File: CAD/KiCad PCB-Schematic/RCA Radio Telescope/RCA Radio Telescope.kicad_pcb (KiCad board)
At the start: 2 copper layers, 60 x 40 mm, 23 parts, among them J2 5V From PoE Splitter, J3 3V Out For LNA, J4 5V Out For Filter Board, J7 USB_A, J8 USB_A, Q1 DMP2008UFG-7, U13 MIC23050-SYML-TR, U14 TPS62133RGTR

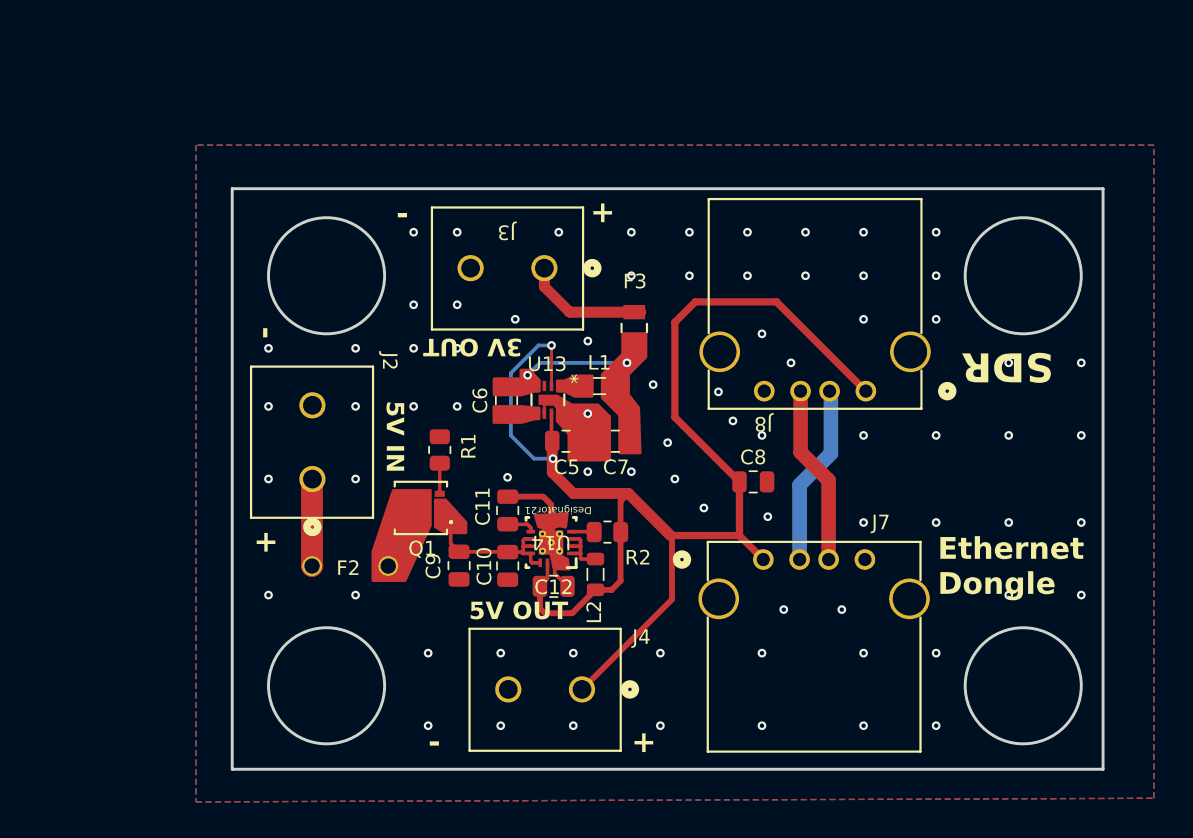
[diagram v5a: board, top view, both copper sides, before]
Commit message: Updated Power/Data Schematic to v1.6 and Power/Data PCB to v1.5
- Added Testpoints to both Schematic and PCB
- Rearranged components on PCB to fit missing diode
- Changed Zener diode and PMOS on Protection Circuit to work with 12V max
- Fixed warnings and errors from DRC
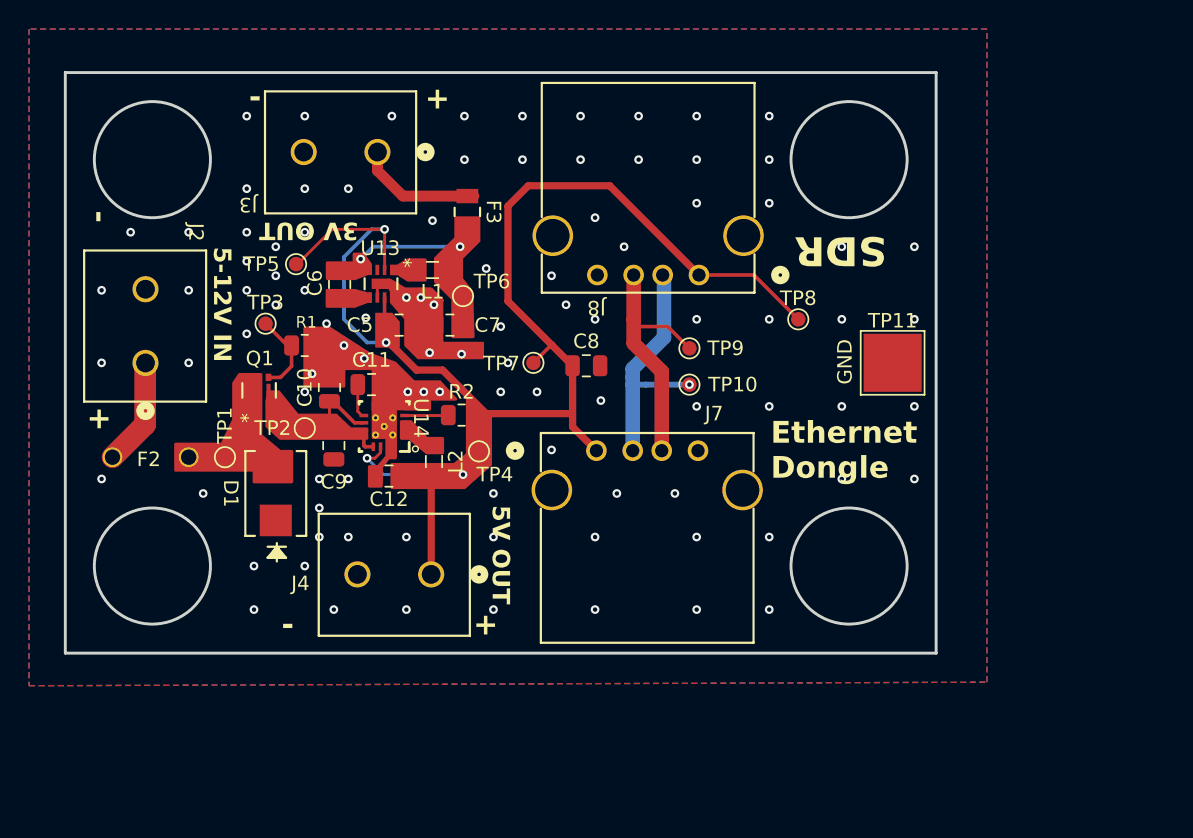
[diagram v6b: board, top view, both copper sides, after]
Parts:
- added D1: SMBJ12A-13-F, Library:SMB_DIO, F.Cu at (28.5, 43.0)
- added TP1: PROCTVIN, TestPoint:TestPoint_Pad_D1.0mm, F.Cu at (25.0, 40.5)
- added TP10: D-USB, TestPoint:TestPoint_Pad_D1.0mm, F.Cu at (57.0, 35.5)
- added TP11: GNDCLIP, TestPoint:TestPoint_Pad_4.0x4.0mm, F.Cu at (71.0, 34.0)
- added TP2: 5VBUCKVIN, TestPoint:TestPoint_Pad_D1.0mm, F.Cu at (30.5, 38.5)
- added TP3: G_PMOS, TestPoint:TestPoint_Pad_D1.0mm, F.Cu at (27.8, 31.3)
- added TP4: 5VBUCKVOUT, TestPoint:TestPoint_Pad_D1.0mm, F.Cu at (42.5, 40.1)
- added TP5: 3VBUCKIN, TestPoint:TestPoint_Pad_D1.0mm, F.Cu at (29.9, 27.2)
- added TP6: 3VBUCKOUT, TestPoint:TestPoint_Pad_D1.0mm, F.Cu at (41.4, 29.4)
- added TP7: 5VOUT, TestPoint:TestPoint_Pad_D1.0mm, F.Cu at (46.2, 34.0)
- added TP8: 5VUSB, TestPoint:TestPoint_Pad_D1.0mm, F.Cu at (64.5, 31.0)
- added TP9: D+USB, TestPoint:TestPoint_Pad_D1.0mm, F.Cu at (57.0, 33.0)
- Q1: value DMP2008UFG-7 -> DMP4047LFDE-7; footprint Library:DMP2008UFG-7_DIO -> Library:U-DFN2020-6_DIO
- U14: footprint TPS62133RGTR:RGT0016C -> Library:RGT0016C
- moved C10 17.4 mm to (32.2, 35.7), turned to 90 degrees
- moved F2 15.7 mm to (20.2, 44.5)
- moved C5 14.0 mm to (37.0, 31.4)
- moved C8 14.0 mm to (49.9, 34.2)
- moved F3 14.0 mm to (41.7, 23.6)
- moved J2 14.0 mm to (19.5, 34.0)
- moved J3 14.0 mm to (35.5, 19.5)
- moved L1 14.0 mm to (39.3, 27.6)
- moved U14 14.0 mm to (36.0, 38.4)
- moved C6 14.0 mm to (32.9, 28.6)
- moved U13 14.0 mm to (35.8, 28.6)
- moved J8 14.0 mm to (57.7, 27.9)
- moved C7 13.9 mm to (40.5, 31.4)
- moved Q1 13.8 mm to (27.3, 35.9), turned to 90 degrees
- moved J7 13.7 mm to (50.6, 40.1)
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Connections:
- U14 pad 18: (no net) -> GND
- U14 pad 19: (no net) -> GND
- U14 pad 20: (no net) -> GND
- U14 pad 21: (no net) -> GND
- U14 pad 22: (no net) -> GND
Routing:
- net GND: track 7.89 -> 1.44 mm, vias 75 -> 98
- net Net-(Q1-S): track 10.9 -> 5.58 mm
- net /PowerDataDistribute/USB_D+_IN: track 12.4 -> 16.9 mm
- net /PowerDataDistribute/USB_D-_IN: track 12.5 -> 16.9 mm, vias 0 -> 1
- net Net-(L2-Pad1): track 4.23 -> 0.00 mm
- net Net-(Q1-G): track 2.11 -> 5.75 mm
- net Net-(U14-PG): track 1.58 -> 3.03 mm
- net /PowerDataDistribute/VDD: track 6.07 -> 7.44 mm
- net +5V: track 97.5 -> 98.1 mm, vias 2 -> 4
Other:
- outline, holes or cut-outs redrawn
- board text added: "5-12V IN"
- board text added: "GND"
- board text added: "PSU ECE Capstone Team 11 - RCA Telescope v1.5"
- board text removed: "5V IN"
- board text removed: "PSU ECE Capstone Team 11 - RCA Telescope v1.1"

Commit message: Updated PowerData PCB to v1.6 and PowerData Schematic to v1.7
- Design Review with Andrew
- Fixed up various parts of PCB parameters
- May consider LDO or filtering for Power IC
- May want to consider a circuit breaker IC for LNA supply
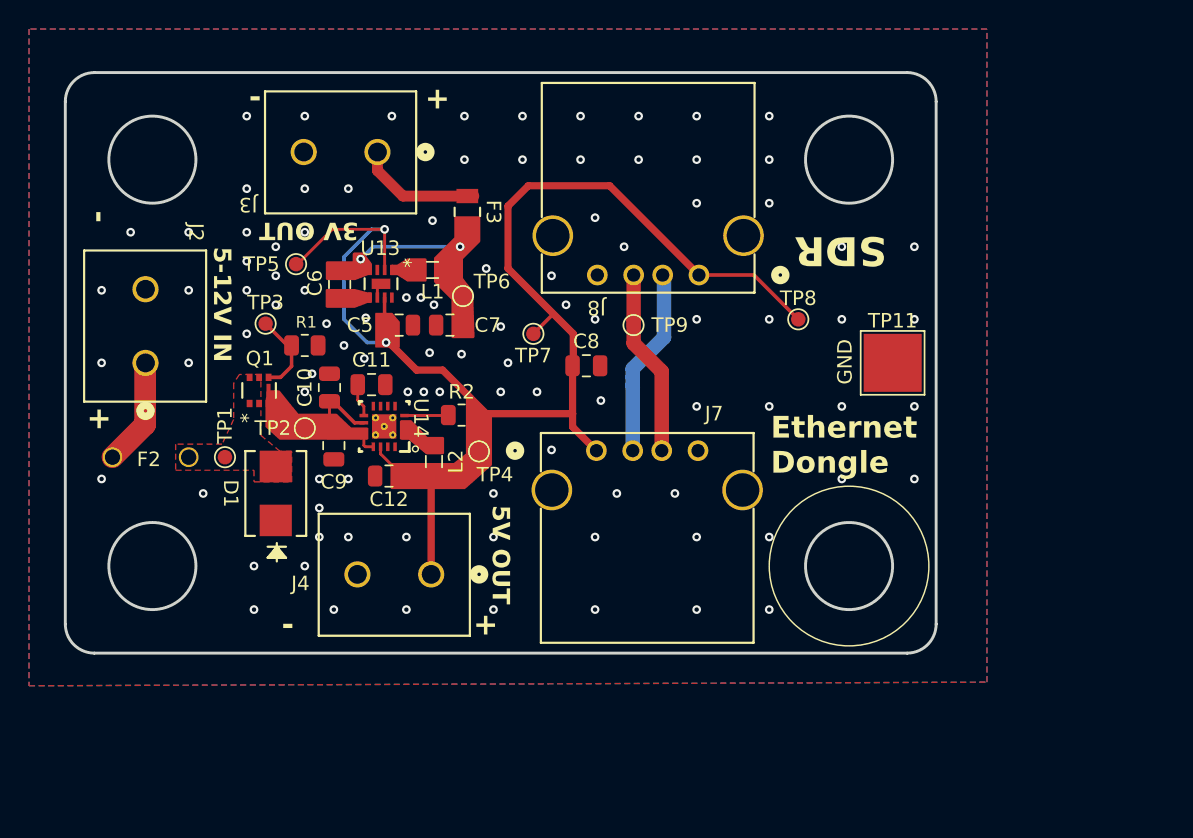
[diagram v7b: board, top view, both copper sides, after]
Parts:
- TP10: moved to B.Cu
- moved TP9 4.17 mm to (53.1, 31.4)
- moved TP10 3.91 mm to (53.1, 35.7), turned to 180 degrees
- moved TP7 2.00 mm to (46.2, 32.0)
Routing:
- net /PowerDataDistribute/USB_D+_IN: track 16.9 -> 12.9 mm
- net /PowerDataDistribute/USB_D-_IN: track 16.9 -> 13.0 mm, vias 1 -> 0
- net +5V: track 98.1 -> 94.3 mm, vias 4 -> 2
- added copper zone on F.Cu, net Net-(Q1-D)
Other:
- outline, holes or cut-outs redrawn
- board text added: "PSU ECE Capstone Team 11 - RCA Telescope v1.6 (3/26/2025)"
- board text removed: "PSU ECE Capstone Team 11 - RCA Telescope v1.5"

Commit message: Updated PowerData Schematic to v1.8 and PCB to v1.7
- Swapped MIC Buck to LDO
- Changed footprint for Buck Inductor to appropriate component
- Rearranged PCB layout to accommodate new inductor
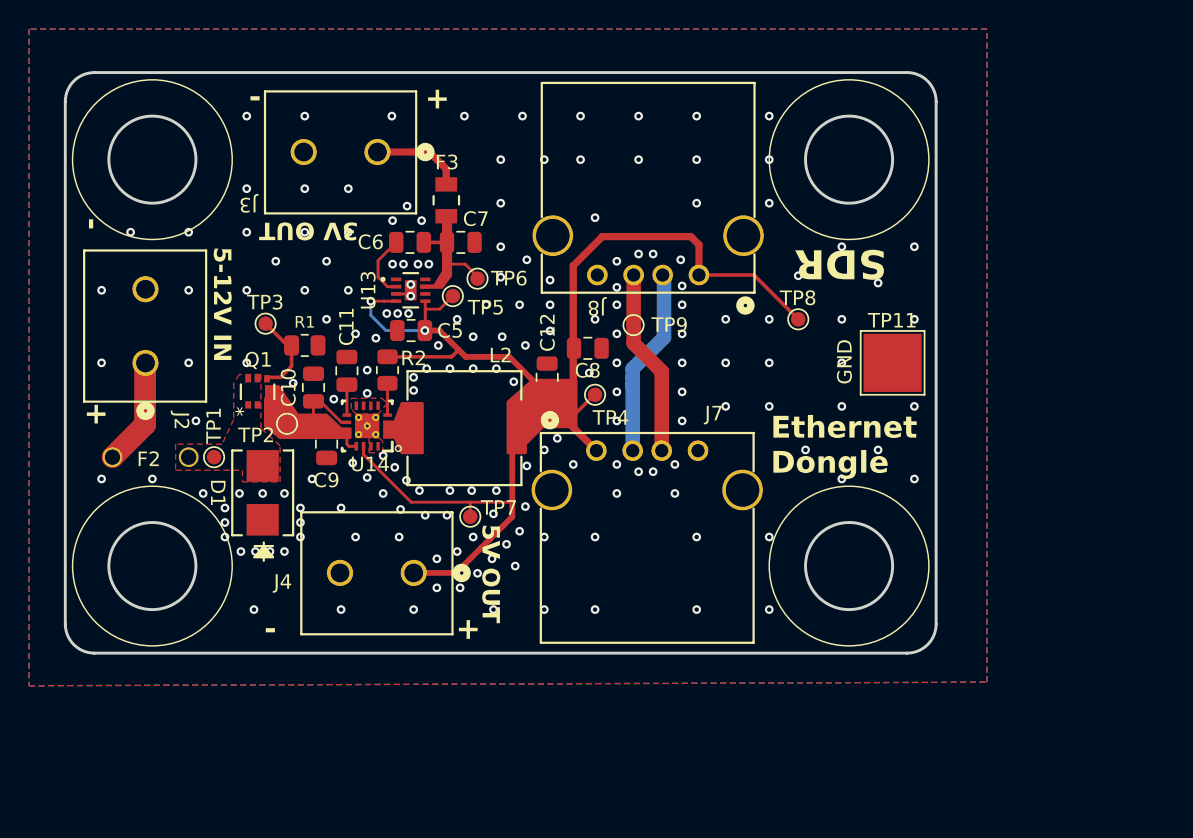
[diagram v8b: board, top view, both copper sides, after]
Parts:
- removed L1: 1 uH, Inductor_SMD:L_0805_2012Metric
- C5, C7: value 4.7 uF -> 1 uF
- C6: value 560 pF -> 10 nf
- L2: footprint Inductor_SMD:L_0805_2012Metric -> Library:IND_CB_DRA73
- TP5: value 3VBUCKIN -> 3VLDOIN
- TP6: value 3VBUCKOUT -> 3VLDOOUT
- U13: value MIC23050-SYML-TR -> MAX8510ETA30+T; footprint Library:MLF-8_ML_MCH -> Library:21-0168E_T822-1_MXM
- moved TP7 13.3 mm to (41.9, 44.6), turned to 90 degrees
- moved C12 12.8 mm to (47.2, 35.0), turned to 90 degrees
- moved TP5 11.0 mm to (40.7, 29.4), turned to 90 degrees
- moved TP4 8.90 mm to (50.5, 36.2)
- moved R2 5.97 mm to (36.2, 34.5), turned to -90 degrees
- moved C7 5.75 mm to (41.2, 25.7), turned to 0 degrees
- moved C6 5.65 mm to (37.8, 25.7), turned to 0 degrees
- moved L2 3.11 mm to (41.5, 38.5), turned to 0 degrees
- moved U13 2.10 mm to (37.8, 29.0), turned to 0 degrees
- moved C11 1.95 mm to (33.4, 34.5), turned to -90 degrees
- moved F3 1.66 mm to (40.2, 22.8)
- moved TP6 1.56 mm to (42.4, 28.2)
- moved TP2 1.26 mm to (29.3, 38.2), turned to 0 degrees
- moved C8 1.20 mm to (50.0, 33.0)
- moved J4 1.20 mm to (38.0, 48.5)
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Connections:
- C6 pad 1: Net-(U13-SNS) -> Net-(U13-BP)
- C6 pad 2: Net-(U13-CFF) -> Net-(U13-OUT)
- C7 pad 1: Net-(U13-SNS) -> Net-(U13-OUT)
- F3 pad 1: Net-(U13-SNS) -> Net-(U13-OUT)
- TP6 pad 1: Net-(U13-SNS) -> Net-(U13-OUT)
- U13 pad 1: Net-(U13-SW) -> unconnected-(U13-NC-Pad1)
- U13 pad 2: +5V -> Net-(U13-BP)
- U13 pad 3: unconnected-(U13-NC-Pad3) -> GND
- U13 pad 4: Net-(U13-SNS) -> +5V
- U13 pad 5: Net-(U13-CFF) -> +5V
- U13 pad 6: GND -> unconnected-(U13-NC-Pad6)
- U13 pad 7: +5V -> Net-(U13-OUT)
- U13 pad 8: GND -> unconnected-(U13-NC-Pad8)
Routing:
- net Net-(U13-SNS): track 7.20 -> 0.00 mm, vias 2 -> 0
- net +5V: track 94.3 -> 89.9 mm
- net Net-(U13-BP): track 0.00 -> 4.43 mm
- net Net-(U13-OUT): track 0.00 -> 3.80 mm
- net +3V0: track 8.65 -> 6.29 mm
- net Net-(U14-PG): track 3.03 -> 2.19 mm
- net GND: track 1.44 -> 1.11 mm, vias 98 -> 181
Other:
- board text added: "PSU ECE Capstone Team 11 - RCA Telescope v1.7 (3/27/2025)"
- board text removed: "PSU ECE Capstone Team 11 - RCA Telescope v1.6 (3/26/2025)"
